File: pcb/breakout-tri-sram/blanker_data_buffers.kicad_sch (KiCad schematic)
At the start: 25 parts, among them U301 74LCX541FT, U302 74LCX541FT, U303 74LCX541FT, U304 74LCX541FT, U305 74LCX541FT, U306 74LCX541FT, U510 74LS573

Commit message: [pci][pci-sram] move to latched buffers
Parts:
- removed U510: 74LS573, symbol 74xx:74LS573
- U301, U302, U303, U304, U305, U306: value 74LCX541FT -> 74LS573; symbol 74xx:74LS541 -> 74xx:74LS573
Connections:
- net +3V3: now also U301.11 (Load), U302.11 (Load), U303.11 (Load), U304.11 (Load), U305.11 (Load), U306.11 (Load)
- net 0_D0: now also U301.15 (Q4); no longer U301.14 (Y4)
- net 0_D1: now also U301.14 (Q5); no longer U301.13 (Y5)
- net 0_D10: now also U304.13 (Q6); no longer U304.12 (Y6)
- net 0_D11: now also U304.12 (Q7); no longer U304.11 (Y7)
- net 0_D2: now also U301.13 (Q6); no longer U301.12 (Y6)
- net 0_D3: now also U301.12 (Q7); no longer U301.11 (Y7)
- net 0_D4: now also U304.19 (Q0); no longer U304.18 (Y0)
- net 0_D5: now also U304.18 (Q1); no longer U304.17 (Y1)
- net 0_D6: now also U304.17 (Q2); no longer U304.16 (Y2)
- net 0_D7: now also U304.16 (Q3); no longer U304.15 (Y3)
- net 0_D8: now also U304.15 (Q4); no longer U304.14 (Y4)
- net 0_D9: now also U304.14 (Q5); no longer U304.13 (Y5)
- net 0_EN#: no longer U301.19 (G2), U304.19 (G2)
- net 1_D0: now also U302.15 (Q4), U303.15 (Q4); no longer U302.14 (Y4), U303.14 (Y4)
- net 1_D1: now also U302.14 (Q5), U303.14 (Q5); no longer U302.13 (Y5), U303.13 (Y5)
- net 1_D10: now also U305.13 (Q6), U306.13 (Q6); no longer U305.12 (Y6), U306.12 (Y6)
- net 1_D11: now also U305.12 (Q7), U306.12 (Q7); no longer U305.11 (Y7), U306.11 (Y7)
- net 1_D2: now also U302.13 (Q6), U303.13 (Q6); no longer U302.12 (Y6), U303.12 (Y6)
- net 1_D3: now also U302.12 (Q7), U303.12 (Q7); no longer U302.11 (Y7), U303.11 (Y7)
- net 1_D4: now also U305.19 (Q0), U306.19 (Q0); no longer U305.18 (Y0), U306.18 (Y0)
- net 1_D5: now also U305.18 (Q1), U306.18 (Q1); no longer U305.17 (Y1), U306.17 (Y1)
- net 1_D6: now also U305.17 (Q2), U306.17 (Q2); no longer U305.16 (Y2), U306.16 (Y2)
- net 1_D7: now also U305.16 (Q3), U306.16 (Q3); no longer U305.15 (Y3), U306.15 (Y3)
- net 1_D8: now also U305.15 (Q4), U306.15 (Q4); no longer U305.14 (Y4), U306.14 (Y4)
- net 1_D9: now also U305.14 (Q5), U306.14 (Q5); no longer U305.13 (Y5), U306.13 (Y5)
- net 1_EN#: no longer U303.19 (G2), U306.19 (G2)
- net 2_EN#: no longer U302.19 (G2), U305.19 (G2)

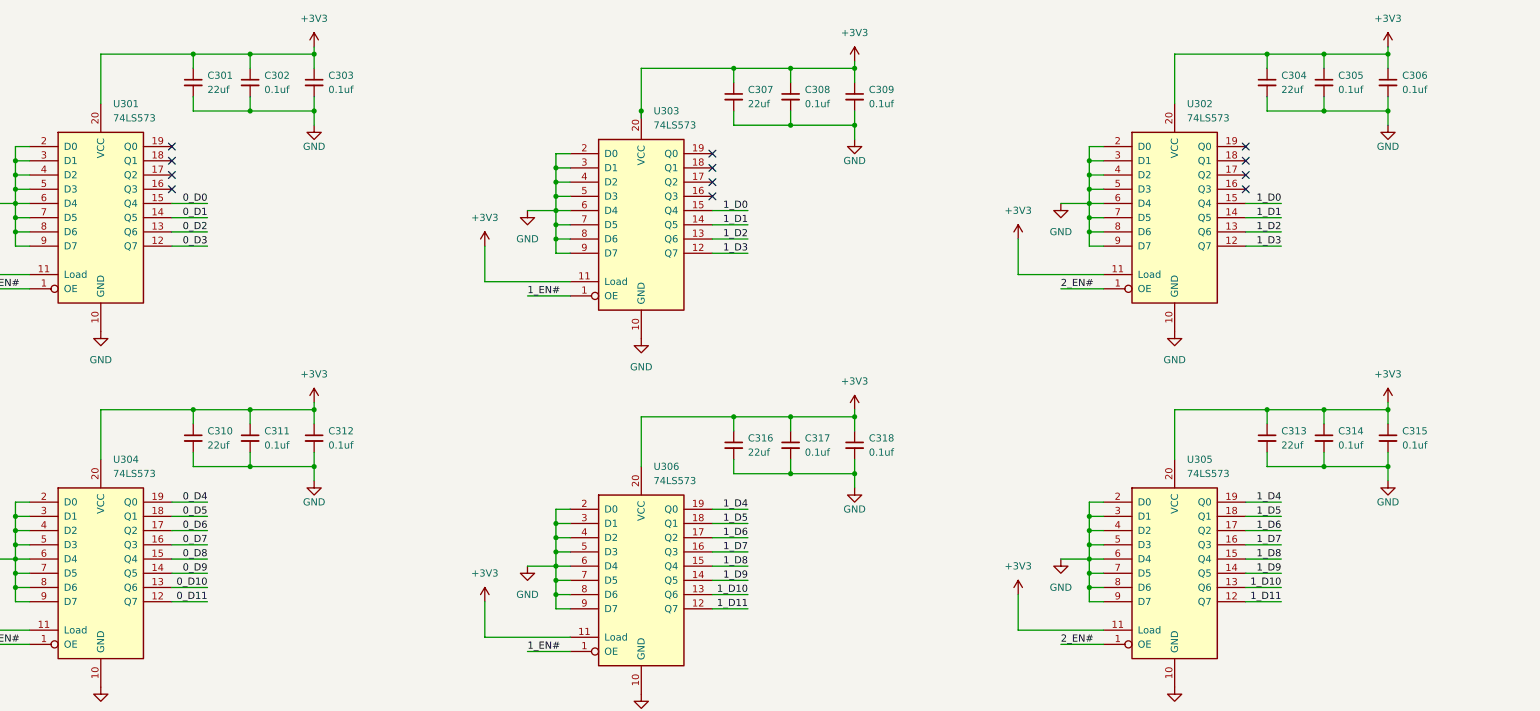
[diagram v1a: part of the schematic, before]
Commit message: [pcb][tri-sram] 3xsram routed
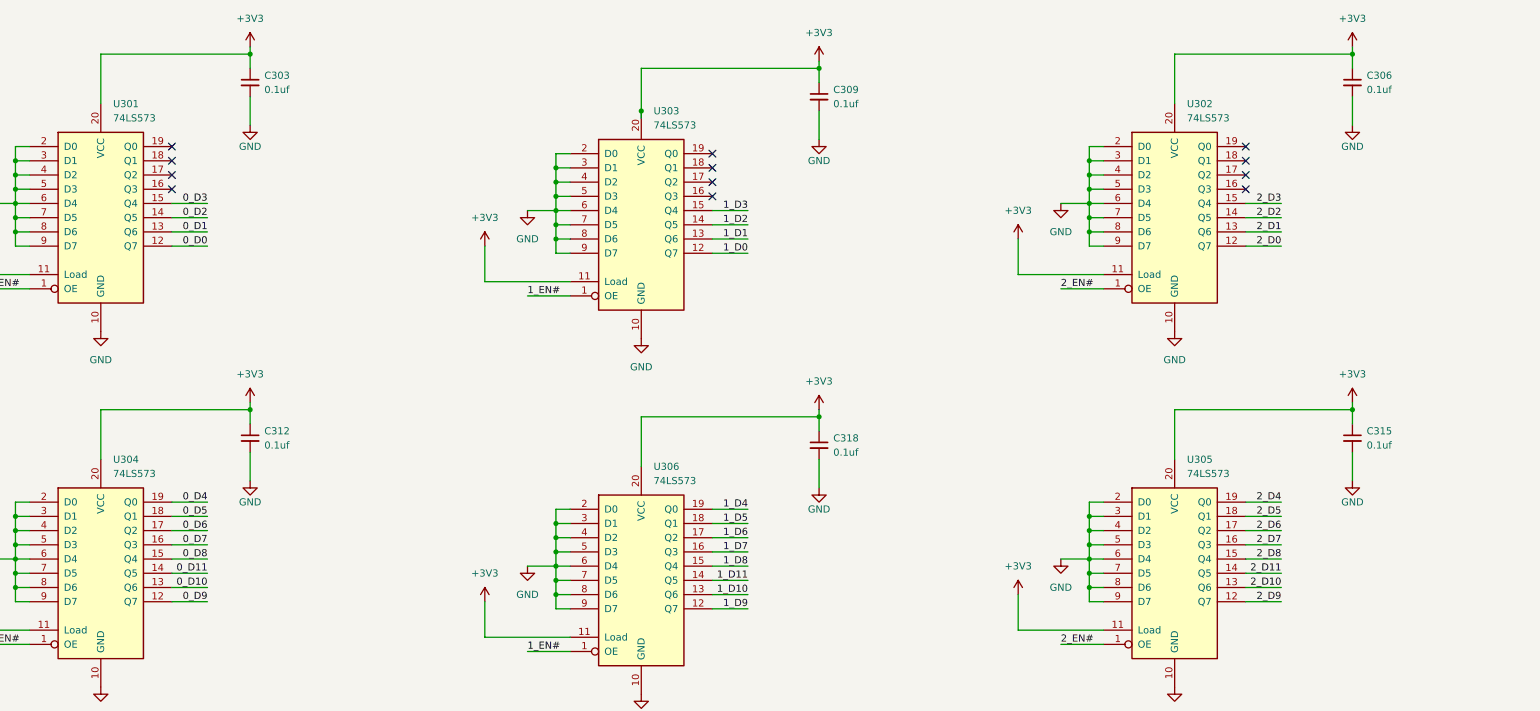
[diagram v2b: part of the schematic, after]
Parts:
- removed C301, C304, C307, C310, C313, C316: 22uf, Capacitor_SMD:C_0603_1608Metric, symbol Device:C_Small
- removed C302, C305, C308, C311, C314, C317: 0.1uf, Capacitor_SMD:C_0402_1005Metric, symbol Device:C_Small
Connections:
- net 0_D0: now also U301.12 (Q7); no longer U301.15 (Q4)
- net 0_D1: now also U301.13 (Q6); no longer U301.14 (Q5)
- net 0_D11: now also U304.14 (Q5); no longer U304.12 (Q7)
- net 0_D2: now also U301.14 (Q5); no longer U301.13 (Q6)
- net 0_D3: now also U301.15 (Q4); no longer U301.12 (Q7)
- net 0_D9: now also U304.12 (Q7); no longer U304.14 (Q5)
- net 1_D0: now also U303.12 (Q7); no longer U302.15 (Q4), U303.15 (Q4)
- net 1_D1: now also U303.13 (Q6); no longer U302.14 (Q5), U303.14 (Q5)
- net 1_D10: no longer U305.13 (Q6)
- net 1_D11: now also U306.14 (Q5); no longer U305.12 (Q7), U306.12 (Q7)
- net 1_D2: now also U303.14 (Q5); no longer U302.13 (Q6), U303.13 (Q6)
- net 1_D3: now also U303.15 (Q4); no longer U302.12 (Q7), U303.12 (Q7)
- net 1_D4: no longer U305.19 (Q0)
- net 1_D5: no longer U305.18 (Q1)
- net 1_D6: no longer U305.17 (Q2)
- net 1_D7: no longer U305.16 (Q3)
- net 1_D8: no longer U305.15 (Q4)
- net 1_D9: now also U306.12 (Q7); no longer U305.14 (Q5), U306.14 (Q5)
- new net 2_D0: U302.12 (Q7)
- new net 2_D1: U302.13 (Q6)
- new net 2_D10: U305.13 (Q6)
- new net 2_D11: U305.14 (Q5)
- new net 2_D2: U302.14 (Q5)
- new net 2_D3: U302.15 (Q4)
- new net 2_D4: U305.19 (Q0)
- new net 2_D5: U305.18 (Q1)
- new net 2_D6: U305.17 (Q2)
- new net 2_D7: U305.16 (Q3)
- new net 2_D8: U305.15 (Q4)
- new net 2_D9: U305.12 (Q7)
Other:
- moved on the sheet: C303, C306, C309, C312, C315, C318

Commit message: [pcb][tri-sram] tri-sram complete
squashed big-bus branch
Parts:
- renumbered C303 to C501, C312 to C502, C309 to C503, C318 to C504, C306 to C505, C315 to C506, U301 to U501, U304 to U502, U303 to U503, U306 to U504, U302 to U505, U305 to U506
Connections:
- net 0_D0: now also U501.19 (Q0); no longer U501.12 (Q7)
- net 0_D1: now also U501.18 (Q1); no longer U501.13 (Q6)
- net 0_D10: now also U502.17 (Q2); no longer U502.13 (Q6)
- net 0_D11: now also U502.16 (Q3); no longer U502.14 (Q5)
- net 0_D2: now also U501.17 (Q2); no longer U501.14 (Q5)
- net 0_D3: now also U501.16 (Q3); no longer U501.15 (Q4)
- net 0_D4: now also U502.12 (Q7); no longer U502.19 (Q0)
- net 0_D5: now also U502.13 (Q6); no longer U502.18 (Q1)
- net 0_D6: now also U502.14 (Q5); no longer U502.17 (Q2)
- net 0_D7: now also U502.15 (Q4); no longer U502.16 (Q3)
- net 0_D8: now also U502.19 (Q0); no longer U502.15 (Q4)
- net 0_D9: now also U502.18 (Q1); no longer U502.12 (Q7)
- net 1_D0: now also U503.19 (Q0); no longer U503.12 (Q7)
- net 1_D1: now also U503.18 (Q1); no longer U503.13 (Q6)
- net 1_D10: now also U504.17 (Q2); no longer U504.13 (Q6)
- net 1_D11: now also U504.16 (Q3); no longer U504.14 (Q5)
- net 1_D2: now also U503.17 (Q2); no longer U503.14 (Q5)
- net 1_D3: now also U503.16 (Q3); no longer U503.15 (Q4)
- net 1_D4: now also U504.12 (Q7); no longer U504.19 (Q0)
- net 1_D5: now also U504.13 (Q6); no longer U504.18 (Q1)
- net 1_D6: now also U504.14 (Q5); no longer U504.17 (Q2)
- net 1_D7: now also U504.15 (Q4); no longer U504.16 (Q3)
- net 1_D8: now also U504.19 (Q0); no longer U504.15 (Q4)
- net 1_D9: now also U504.18 (Q1); no longer U504.12 (Q7)
- net 2_D0: now also U505.19 (Q0); no longer U505.12 (Q7)
- net 2_D1: now also U505.18 (Q1); no longer U505.13 (Q6)
- net 2_D10: now also U506.17 (Q2); no longer U506.13 (Q6)
- net 2_D11: now also U506.16 (Q3); no longer U506.14 (Q5)
- net 2_D2: now also U505.17 (Q2); no longer U505.14 (Q5)
- net 2_D3: now also U505.16 (Q3); no longer U505.15 (Q4)
- net 2_D4: now also U506.12 (Q7); no longer U506.19 (Q0)
- net 2_D5: now also U506.13 (Q6); no longer U506.18 (Q1)
- net 2_D6: now also U506.14 (Q5); no longer U506.17 (Q2)
- net 2_D7: now also U506.15 (Q4); no longer U506.16 (Q3)
- net 2_D8: now also U506.19 (Q0); no longer U506.15 (Q4)
- net 2_D9: now also U506.18 (Q1); no longer U506.12 (Q7)
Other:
- moved on the sheet: C503, C504, U503, U504

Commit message: [pcb][tri-sram] add part numbers
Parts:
- U501, U502, U503, U504, U505, U506: Digi-Key Part Number (none) -> 264-74LCX541FT(AE)CT-ND
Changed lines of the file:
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@@
+			)
+		)
+		(property "Digi-Key Part Number" "264-74LCX541FT(AE)CT-ND"
+			(at 67.31 166.37 0)
+			(effects
+				(font
+					(size 1.27 1.27)
+				)
+				(hide yes)
 			)
 		)
@@
 			)
 		)
+		(property "Digi-Key Part Number" "264-74LCX541FT(AE)CT-ND"
+			(at 163.83 102.87 0)
+			(effects
+				(font
+					(size 1.27 1.27)
+				)
+				(hide yes)
+			)
+		)
 		(pin "5"
 		)
@@
 			)
 		)
+		(property "Digi-Key Part Number" "264-74LCX541FT(AE)CT-ND"
+			(at 163.83 166.37 0)
+			(effects
+				(font
+					(size 1.27 1.27)
+				)
+				(hide yes)
+			)
+		)
 		(pin "5"
 		)
@@
 			)
 		)
+		(property "Digi-Key Part Number" "264-74LCX541FT(AE)CT-ND"
+			(at 67.31 102.87 0)
+			(effects
+				(font
+					(size 1.27 1.27)
+				)
+				(hide yes)
+			)
+		)
 		(pin "5"
 		)
@@
 			)
 		)
+		(property "Digi-Key Part Number" "264-74LCX541FT(AE)CT-ND"
+			(at 259.08 166.37 0)
+			(effects
+				(font
+					(size 1.27 1.27)
+				)
+				(hide yes)
+			)
+		)
 		(pin "5"
 		)
@@
 			(at 259.08 102.87 0)
 			(effects
+				(font
+					(size 1.27 1.27)
+				)
+				(hide yes)
+			)
+		)
+		(property "Digi-Key Part Number" "264-74LCX541FT(AE)CT-ND"
+			(at 259.08 102.87 0)
+			(effects
